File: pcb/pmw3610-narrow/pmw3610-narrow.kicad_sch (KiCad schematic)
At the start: 16 parts, among them J2 vik-module-connector, U1 MG6208T3-18, U2 PMW3610

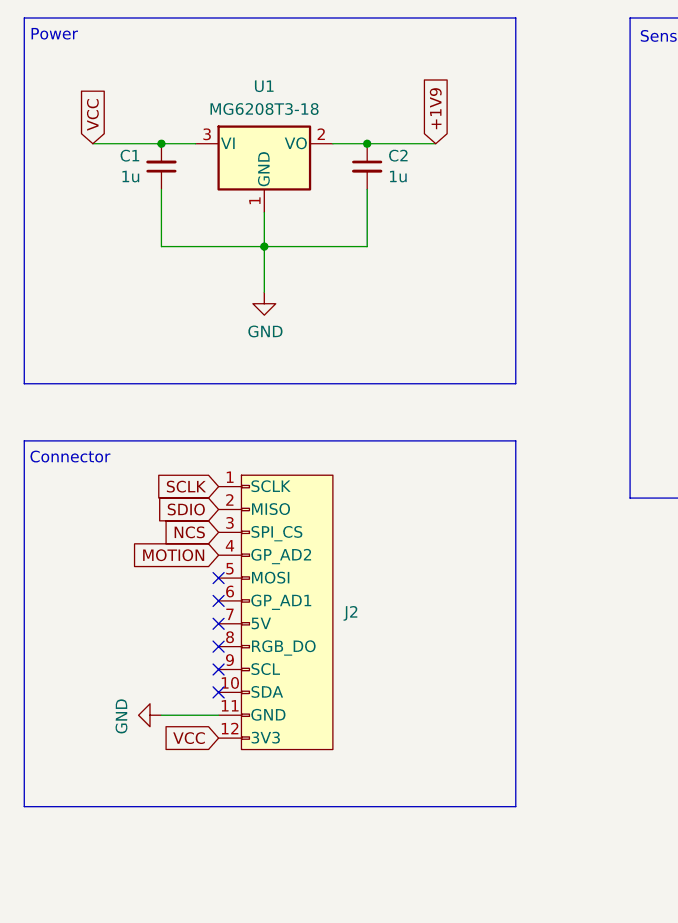
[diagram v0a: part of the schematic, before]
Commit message: Change voltage regulator on PMW3610-narrow.
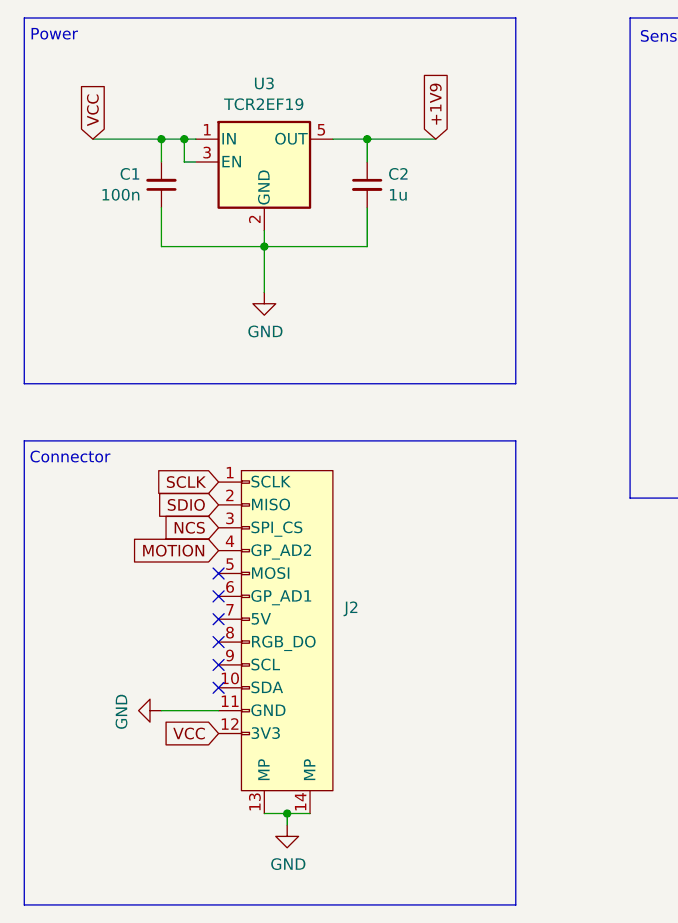
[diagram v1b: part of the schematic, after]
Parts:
- removed U1: MG6208T3-18, Package_TO_SOT_SMD:SOT-23, symbol Regulator_Linear:MCP1700x-180xxTT
- added U3: TCR2EF19, Package_TO_SOT_SMD:SOT-23-5, symbol Regulator_Linear:TLV70218_SOT23-5
- C1: value 1u -> 100n
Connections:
- net +1V9: now also U3.5 (OUT)
- net GND: now also J2.13 (MP), J2.14 (MP), U3.2 (GND)
- net VCC: now also U3.1 (IN), U3.3 (EN)
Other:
- moved on the sheet: C1, C2

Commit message: Change passives to 0805 footprint.
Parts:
- C1, C2, C3, C4, C5, C6, C7, C8, C9: footprint Capacitor_SMD:C_0603_1608Metric_Pad1.08x0.95mm_HandSolder -> Capacitor_SMD:C_0805_2012Metric_Pad1.18x1.45mm_HandSolder
- R1: footprint Resistor_SMD:R_0603_1608Metric_Pad0.98x0.95mm_HandSolder -> Resistor_SMD:R_0805_2012Metric_Pad1.20x1.40mm_HandSolder
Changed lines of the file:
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@@
 			)
 		)
-		(property "Footprint" "Capacitor_SMD:C_0603_1608Metric_Pad1.08x0.95mm_HandSolder"
+		(property "Footprint" "Capacitor_SMD:C_0805_2012Metric_Pad1.18x1.45mm_HandSolder"
 			(at 57.15 35.56 0)
 			(hide yes)
@@
 			)
 		)
-		(property "Footprint" "Capacitor_SMD:C_0603_1608Metric_Pad1.08x0.95mm_HandSolder"
+		(property "Footprint" "Capacitor_SMD:C_0805_2012Metric_Pad1.18x1.45mm_HandSolder"
 			(at 99.06 44.958 0)
 			(hide yes)
@@
 			)
 		)
-		(property "Footprint" "Capacitor_SMD:C_0603_1608Metric_Pad1.08x0.95mm_HandSolder"
+		(property "Footprint" "Capacitor_SMD:C_0805_2012Metric_Pad1.18x1.45mm_HandSolder"
 			(at 171.45 34.798 0)
 			(hide yes)
@@
 			)
 		)
-		(property "Footprint" "Capacitor_SMD:C_0603_1608Metric_Pad1.08x0.95mm_HandSolder"
+		(property "Footprint" "Capacitor_SMD:C_0805_2012Metric_Pad1.18x1.45mm_HandSolder"
 			(at 154.94 24.638 0)
 			(hide yes)
@@
 			)
 		)
-		(property "Footprint" "Capacitor_SMD:C_0603_1608Metric_Pad1.08x0.95mm_HandSolder"
+		(property "Footprint" "Capacitor_SMD:C_0805_2012Metric_Pad1.18x1.45mm_HandSolder"
 			(at 154.94 38.608 0)
 			(hide yes)
@@
 			)
 		)
-		(property "Footprint" "Capacitor_SMD:C_0603_1608Metric_Pad1.08x0.95mm_HandSolder"
+		(property "Footprint" "Capacitor_SMD:C_0805_2012Metric_Pad1.18x1.45mm_HandSolder"
 			(at 34.29 35.56 0)
 			(hide yes)
@@
 			)
 		)
-		(property "Footprint" "Resistor_SMD:R_0603_1608Metric_Pad0.98x0.95mm_HandSolder"
+		(property "Footprint" "Resistor_SMD:R_0805_2012Metric_Pad1.20x1.40mm_HandSolder"
 			(at 104.648 55.372 90)
 			(hide yes)
@@
 			)
 		)
-		(property "Footprint" "Capacitor_SMD:C_0603_1608Metric_Pad1.08x0.95mm_HandSolder"
+		(property "Footprint" "Capacitor_SMD:C_0805_2012Metric_Pad1.18x1.45mm_HandSolder"
 			(at 170.18 51.308 0)
 			(hide yes)
@@
 			)
 		)
-		(property "Footprint" "Capacitor_SMD:C_0603_1608Metric_Pad1.08x0.95mm_HandSolder"
+		(property "Footprint" "Capacitor_SMD:C_0805_2012Metric_Pad1.18x1.45mm_HandSolder"
 			(at 179.07 34.798 0)
 			(hide yes)
@@
 			)
 		)
-		(property "Footprint" "Capacitor_SMD:C_0603_1608Metric_Pad1.08x0.95mm_HandSolder"
+		(property "Footprint" "Capacitor_SMD:C_0805_2012Metric_Pad1.18x1.45mm_HandSolder"
 			(at 162.56 51.308 0)
 			(hide yes)
